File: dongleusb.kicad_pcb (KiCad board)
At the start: 2 copper layers, 13 parts, among them P7 UART_GROVE, U1 FT230XS, U2 HM-11

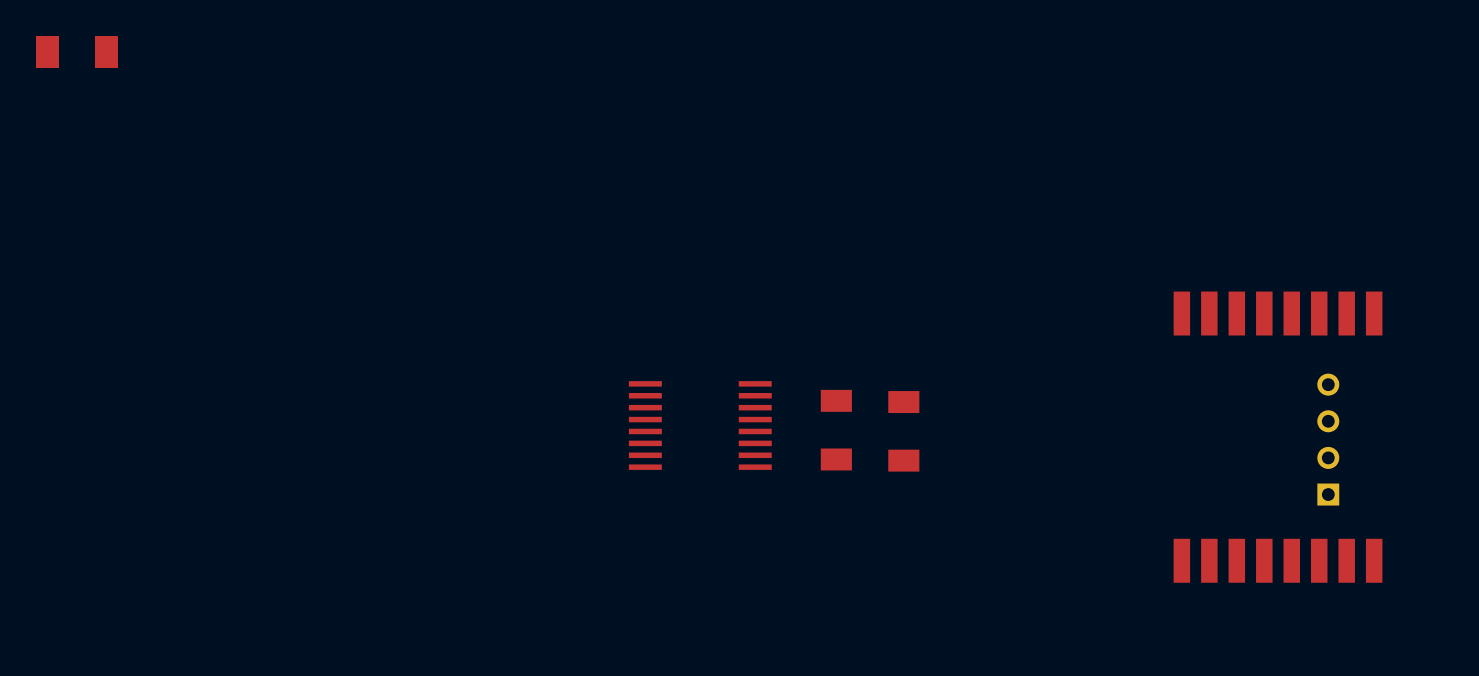
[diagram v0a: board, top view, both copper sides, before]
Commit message: Added LEDs informations. Added USB footprint. Placed some components into layout.
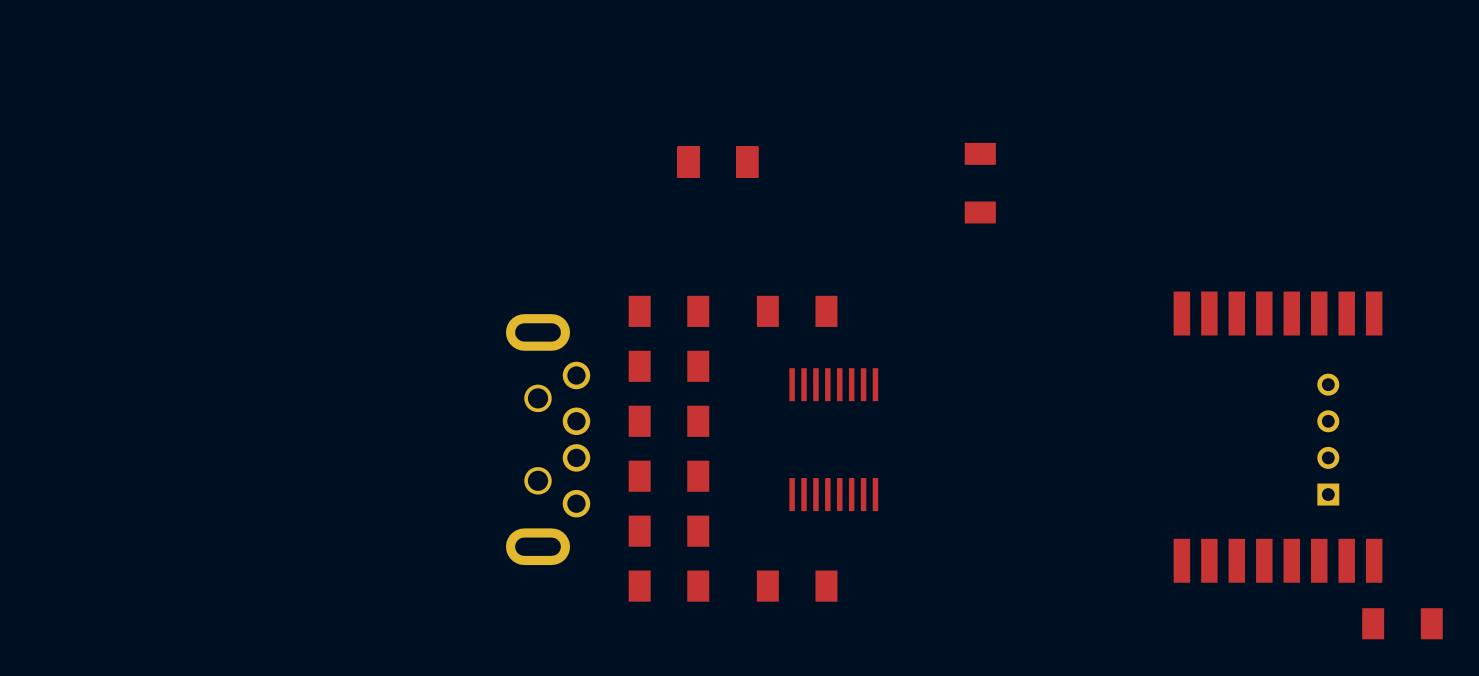
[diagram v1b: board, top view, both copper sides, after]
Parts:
- added D1: LED, W-LED-1206, F.Cu at (178.1, 107.1)
- added D2: LED, W-LED-1206, F.Cu at (138.0, 90.0)
- added D3: LED, W-LED-1206, F.Cu at (138.0, 105.0)
- added P1: USB, W-CONN-USB-A-MULTICOMP-THT, F.Cu at (123.0, 97.0)
- moved R5 49.0 mm to (145.0, 105.0)
- moved C1 41.6 mm to (138.0, 102.0)
- moved R1 39.8 mm to (138.0, 99.0)
- moved C2 38.1 mm to (138.0, 96.0)
- moved R2 36.6 mm to (138.0, 93.0)
- moved C4 35.5 mm to (140.7, 81.8)
- moved R3 35.5 mm to (140.7, 81.8)
- moved R6 35.5 mm to (140.7, 81.8)
- moved C3 14.2 mm to (155.0, 83.0)
- moved U1 7.33 mm to (147.0, 97.0), turned to 0 degrees
- moved R4 6.83 mm to (145.0, 90.0), turned to 0 degrees

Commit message: Placed all components. Added some commercial informations of communications modules.
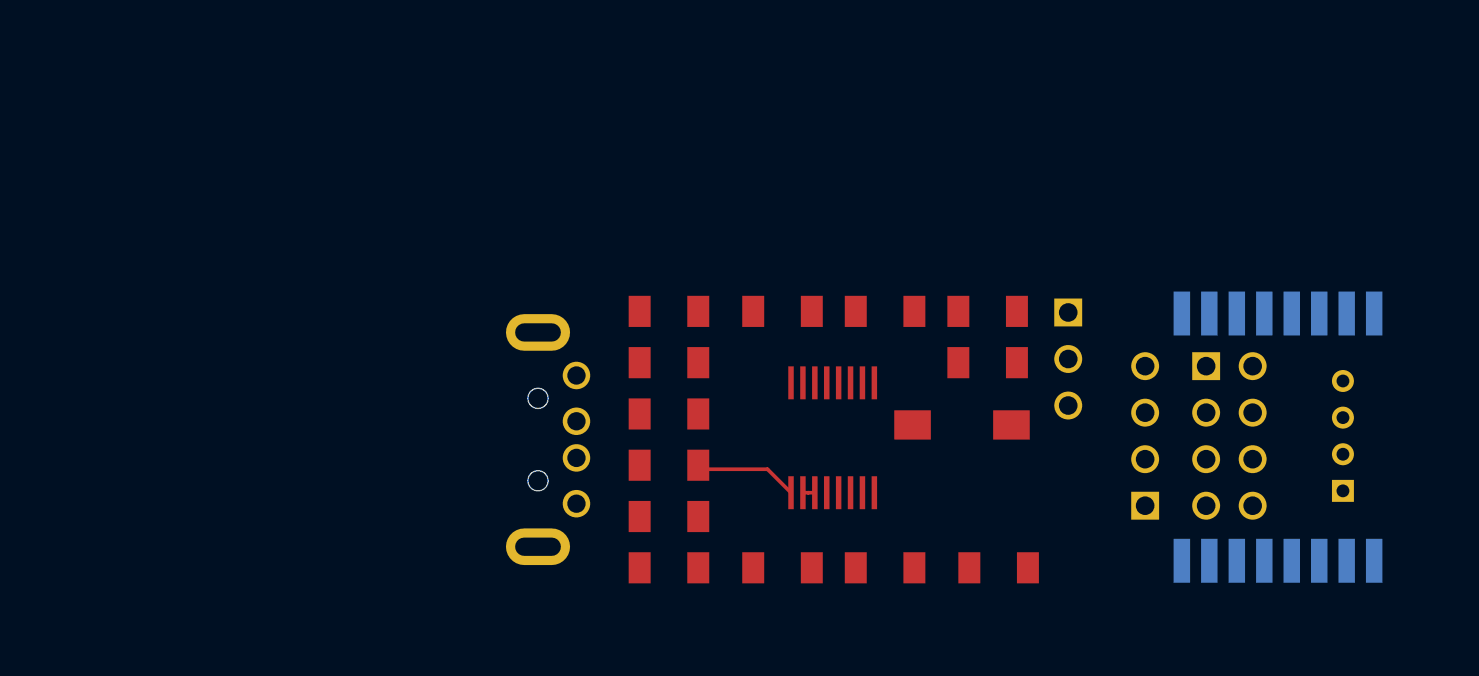
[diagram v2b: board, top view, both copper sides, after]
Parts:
- added G***: OSHW-logo_silkscreen-front_3mm, OSHW-logo_silkscreen-front_3mm, F.Cu at (160.0, 99.4)
- added JP1: ENABLE_VCC, W-CONN-3x1-STRIP, F.Cu at (159.8, 92.6)
- added P5: ESP8266, W-CONN-4x2-STRIP, F.Cu at (168.6, 96.8)
- added P6: UART_TERMINAL, W-CONN-4x1-STRIP, F.Cu at (164.0, 96.8)
- added SW1: RESET, W-SWITCH-EVQPE1, F.Cu at (154.0, 96.2)
- U2: moved to B.Cu
- moved R3 24.0 mm to (149.8, 104.0), turned to 180 degrees
- moved D1 22.3 mm to (156.0, 104.0), turned to 180 degrees
- moved C4 18.4 mm to (155.4, 92.8), turned to 180 degrees
- moved R6 16.8 mm to (155.4, 90.0), turned to 180 degrees
- moved R5 15.0 mm to (144.2, 90.0)
- moved D3 15.0 mm to (138.0, 90.0)
- moved R4 14.0 mm to (144.2, 104.0)
- moved D2 14.0 mm to (138.0, 104.0)
- moved C3 8.72 mm to (149.8, 90.0), turned to 0 degrees
- moved P7 0.82 mm to (174.8, 96.8)
- moved C1 0.80 mm to (138.0, 101.2)
- moved R1 0.60 mm to (138.0, 98.4)
- moved C2 0.40 mm to (138.0, 95.6)
- moved R2 0.20 mm to (138.0, 92.8)
- moved U1 0.12 mm to (146.9, 96.9), turned to 180 degrees
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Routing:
- net N-0000031: track 0.00 -> 5.60 mm
- net +3.3V: track 0.00 -> 0.65 mm
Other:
- net class Default: clearance 0.254 -> 0.2; trace_width 0.254 -> 0.2; via_dia 0.889 -> 0.8; via_drill 0.635 -> 0.4
- rule trace_clearance: 0.254 -> 0.2
- rule trace_min: 0.254 -> 0.2
- rule via_min_drill: 0.508 -> 0.4
- rule via_min_size: 0.889 -> 0.8
- board text added: "A"
- board text added: "B"
- board text added: "W001-0 USB2World CC 4.0 BY-SA"

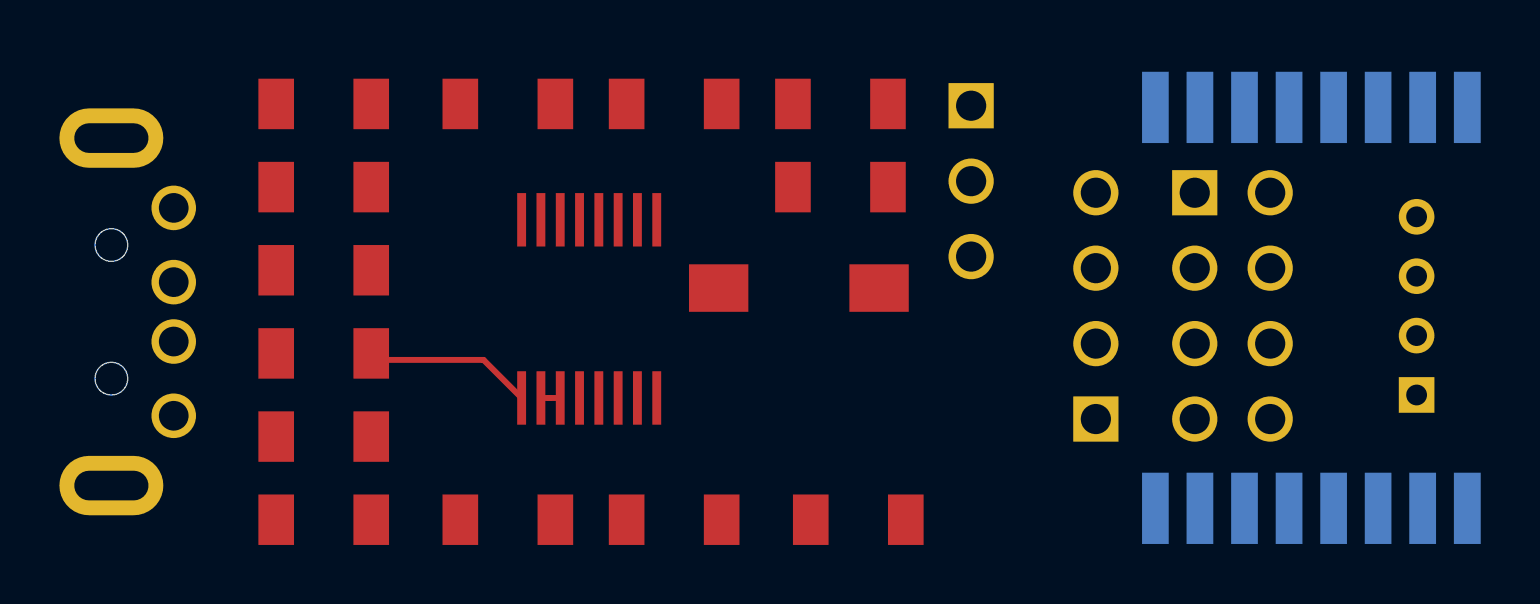
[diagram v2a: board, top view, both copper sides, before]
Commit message: Connected all nets into layout.
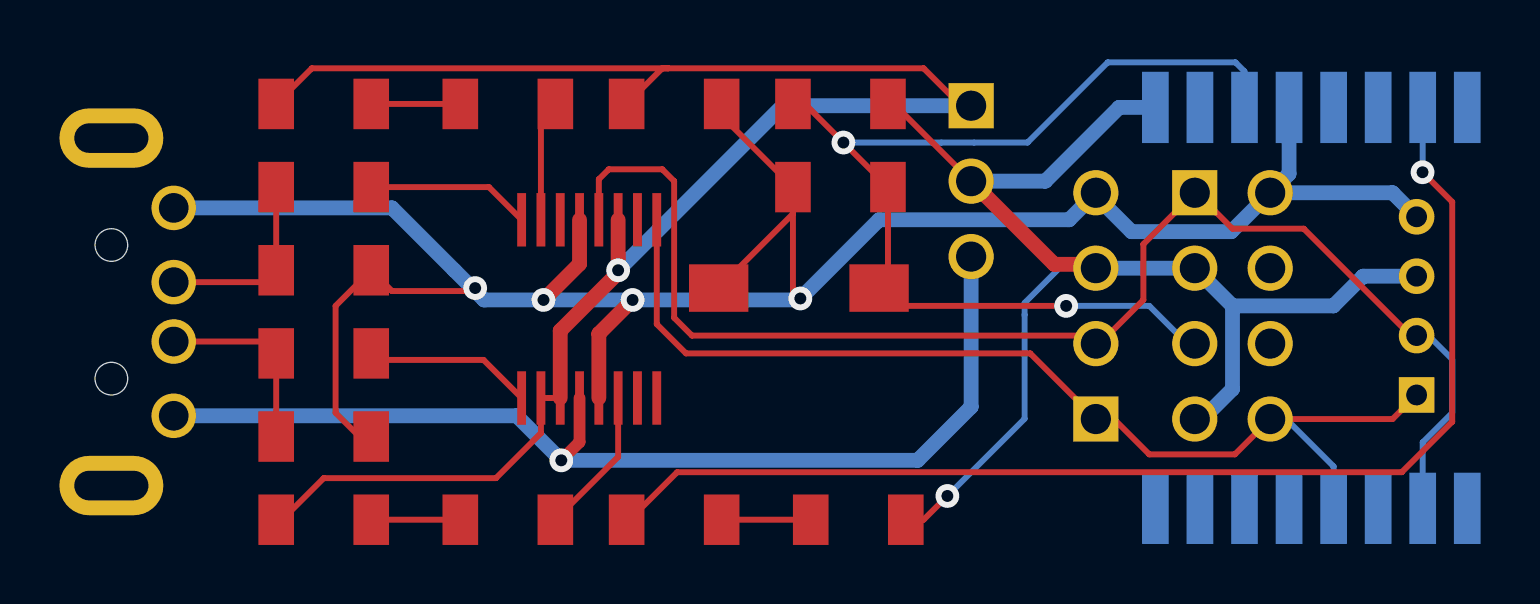
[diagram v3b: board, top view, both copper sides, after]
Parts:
- moved G*** 4.70 mm to (162.3, 103.5)
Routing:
- net GND: track 0.00 -> 79.0 mm, vias 0 -> 4
- net +3.3V: track 0.65 -> 59.3 mm, vias 0 -> 1
- net /UART_TX: track 0.00 -> 46.3 mm
- net /VCC: track 0.00 -> 44.9 mm, vias 0 -> 1
- net /LED_COMM: track 0.00 -> 40.2 mm, vias 0 -> 1
- net /UART_RX: track 0.00 -> 36.0 mm
- net +5V: track 0.00 -> 35.6 mm, vias 0 -> 1
- net /RESET: track 0.00 -> 35.3 mm, vias 0 -> 2
- net N-0000033: track 0.00 -> 6.42 mm
- net N-0000030: track 0.00 -> 6.42 mm
- net N-0000032: track 0.00 -> 5.52 mm
- net N-0000018: track 0.00 -> 4.97 mm
- net N-0000017: track 0.00 -> 4.10 mm
- net N-0000021: track 0.00 -> 3.00 mm
- net N-0000019: track 0.00 -> 3.00 mm
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
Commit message: Added my logo
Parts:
- added VAL: REF, W-LOGO-4MM, F.Cu at (160.1, 99.0)
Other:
- rule pad_to_mask_clearance: 0 -> 0.1
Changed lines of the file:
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@@
     (tracks 176)
     (zones 0)
-    (modules 22)
+    (modules 23)
     (nets 18)
   )
@@
     (pad_size 1.524 1.524)
     (pad_drill 1.016)
-    (pad_to_mask_clearance 0)
+    (pad_to_mask_clearance 0.1)
+    (solder_mask_min_width 0.1)
     (aux_axis_origin 0 0)
     (visible_elements 7FFFFFBF)
@@
       (psa4output false)
       (plotreference true)
-      (plotvalue true)
+      (plotvalue false)
       (plotothertext true)
       (plotinvisibletext false)
-      (padsonsilk true)
+      (padsonsilk false)
       (subtractmaskfromsilk false)
-      (outputformat 5)
+      (outputformat 1)
       (mirror false)
       (drillshape 0)
@@
       (xy -0.90932 1.3462)) (layer Serigrafia.Fronte) (width 0.00254))
   )
+  (module W-LOGO-4MM (layer Rame.Fronte)
+    (at 160.1 99)
+    (fp_text reference VAL (at 0 0) (layer Serigrafia.Fronte) hide
+      (effects (font (size 0.381 0.381) (thickness 0.127)))
+    )
+    (fp_text value REF (at 0 0) (layer Serigrafia.Fronte) hide
+      (effects (font (size 0.381 0.381) (thickness 0.127)))
+    )
+    (fp_poly (pts (xy 1.90754 -0.00508) (xy 1.89738 0.20066) (xy 1.8669 0.40132) (xy 1.8161 0.5969)
+      (xy 1.74244 0.7874) (xy 1.64846 0.96774) (xy 1.53416 1.13538) (xy 1.44018 1.24714)
+      (xy 1.44018 1.01092) (xy 1.43764 0.99568) (xy 1.43002 0.96012) (xy 1.41732 0.90424)
+      (xy 1.39954 0.82804) (xy 1.37922 0.73914) (xy 1.35636 0.63246) (xy 1.32842 0.51562)
+      (xy 1.30048 0.38862) (xy 1.27 0.25146) (xy 1.23698 0.10922) (xy 1.20142 -0.0381)
+      (xy 1.1684 -0.18796) (xy 1.13284 -0.34036) (xy 1.09982 -0.49022) (xy 1.06426 -0.63754)
+      (xy 1.03124 -0.77978) (xy 1.00076 -0.9144) (xy 0.97028 -1.0414) (xy 0.94488 -1.1557)
+      (xy 0.91948 -1.25984) (xy 0.89916 -1.34874) (xy 0.88138 -1.4224) (xy 0.86868 -1.47574)
+      (xy 0.86106 -1.50876) (xy 0.85852 -1.52146) (xy 0.84582 -1.51892) (xy 0.81788 -1.50368)
+      (xy 0.7747 -1.48082) (xy 0.7239 -1.45034) (xy 0.70612 -1.44018) (xy 0.64262 -1.40208)
+      (xy 0.59944 -1.37414) (xy 0.57404 -1.35382) (xy 0.56388 -1.33858) (xy 0.56134 -1.3335)
+      (xy 0.56642 -1.31826) (xy 0.57404 -1.28016) (xy 0.58674 -1.22428) (xy 0.60452 -1.14808)
+      (xy 0.62738 -1.05664) (xy 0.65278 -0.9525) (xy 0.68072 -0.83312) (xy 0.7112 -0.70612)
+      (xy 0.74422 -0.5715) (xy 0.76962 -0.47498) (xy 0.80264 -0.33528) (xy 0.83566 -0.2032)
+      (xy 0.8636 -0.07874) (xy 0.89154 0.03302) (xy 0.9144 0.13208) (xy 0.93472 0.2159)
+      (xy 0.94996 0.28448) (xy 0.96266 0.33528) (xy 0.96774 0.36322) (xy 0.97028 0.37084)
+      (xy 0.96012 0.36322) (xy 0.93472 0.3429) (xy 0.89154 0.3048) (xy 0.8382 0.25654)
+      (xy 0.76962 0.19558) (xy 0.69342 0.12446) (xy 0.60452 0.04572) (xy 0.508 -0.04318)
+      (xy 0.4064 -0.13716) (xy 0.30734 -0.22606) (xy -0.35052 -0.83312) (xy -0.40132 -0.80264)
+      (xy -0.43688 -0.77978) (xy -0.44704 -0.75946) (xy -0.44704 -0.75438) (xy -0.43942 -0.72136)
+      (xy -0.42926 -0.67056) (xy -0.41402 -0.59944) (xy -0.3937 -0.51562) (xy -0.37338 -0.4191)
+      (xy -0.34798 -0.31242) (xy -0.32258 -0.19558) (xy -0.29718 -0.0762) (xy -0.26924 0.04826)
+      (xy -0.2413 0.17272) (xy -0.21336 0.29718) (xy -0.18796 0.4191) (xy -0.16256 0.5334)
+      (xy -0.1397 0.64008) (xy -0.11684 0.7366) (xy -0.09906 0.82042) (xy -0.08382 0.889)
+      (xy -0.07366 0.9398) (xy -0.06604 0.97028) (xy -0.06604 0.98044) (xy -0.0762 0.97282)
+      (xy -0.1016 0.94996) (xy -0.1397 0.91186) (xy -0.19558 0.86106) (xy -0.26162 0.79756)
+      (xy -0.33782 0.7239) (xy -0.42418 0.64262) (xy -0.51816 0.55118) (xy -0.61722 0.45466)
+      (xy -0.70866 0.3683) (xy -0.8128 0.2667) (xy -0.91186 0.17272) (xy -1.00584 0.08382)
+      (xy -1.0922 0.00254) (xy -1.1684 -0.07112) (xy -1.23444 -0.13208) (xy -1.28524 -0.18288)
+      (xy -1.32588 -0.21844) (xy -1.34874 -0.2413) (xy -1.3589 -0.24638) (xy -1.37414 -0.2413)
+      (xy -1.40462 -0.22352) (xy -1.44526 -0.20066) (xy -1.49352 -0.17526) (xy -1.54178 -0.14478)
+      (xy -1.58496 -0.11938) (xy -1.62052 -0.09398) (xy -1.64084 -0.07874) (xy -1.64592 -0.07112)
+      (xy -1.6383 -0.0635) (xy -1.61036 -0.0381) (xy -1.56972 0.00254) (xy -1.51384 0.05334)
+      (xy -1.4478 0.11684) (xy -1.36906 0.1905) (xy -1.28016 0.27178) (xy -1.18364 0.36068)
+      (xy -1.08204 0.45466) (xy -0.97536 0.55372) (xy -0.8636 0.65786) (xy -0.7493 0.762)
+      (xy -0.635 0.86868) (xy -0.5207 0.97282) (xy -0.40894 1.07442) (xy -0.30226 1.17348)
+      (xy -0.19812 1.26746) (xy -0.1016 1.35636) (xy -0.0127 1.43764) (xy 0.06604 1.5113)
+      (xy 0.13462 1.5748) (xy 0.19304 1.6256) (xy 0.23622 1.6637) (xy 0.26416 1.6891)
+      (xy 0.27432 1.69672) (xy 0.27432 1.69672) (xy 0.2921 1.69164) (xy 0.32004 1.6764)
+      (xy 0.32766 1.67386) (xy 0.35306 1.65608) (xy 0.36068 1.6383) (xy 0.35814 1.60782)
+      (xy 0.3556 1.60274) (xy 0.35052 1.58242) (xy 0.3429 1.53924) (xy 0.3302 1.47828)
+      (xy 0.31242 1.39954) (xy 0.2921 1.3081) (xy 0.26924 1.20396) (xy 0.24638 1.0922)
+      (xy 0.22098 0.97282) (xy 0.19304 0.8509) (xy 0.16764 0.72644) (xy 0.14224 0.60452)
+      (xy 0.1143 0.48514) (xy 0.09144 0.37338) (xy 0.06858 0.26924) (xy 0.04826 0.1778)
+      (xy 0.03302 0.09906) (xy 0.02032 0.0381) (xy 0.01016 -0.00508) (xy 0.00762 -0.02286)
+      (xy -0.00254 -0.0635) (xy -0.00508 -0.08382) (xy 0 -0.0889) (xy 0.01016 -0.08382)
+      (xy 0.01016 -0.08128) (xy 0.02286 -0.07112) (xy 0.05334 -0.04572) (xy 0.09652 -0.00762)
+      (xy 0.15748 0.04318) (xy 0.2286 0.10668) (xy 0.30988 0.1778) (xy 0.40132 0.25654)
+      (xy 0.50292 0.3429) (xy 0.60706 0.43434) (xy 0.69342 0.508) (xy 1.35382 1.08204)
+      (xy 1.397 1.05664) (xy 1.42494 1.03632) (xy 1.43764 1.016) (xy 1.44018 1.01092)
+      (xy 1.44018 1.24714) (xy 1.40208 1.29286) (xy 1.24968 1.4351) (xy 1.08458 1.55956)
+      (xy 0.93218 1.651) (xy 0.76708 1.7272) (xy 0.59436 1.7907) (xy 0.42418 1.83642)
+      (xy 0.39624 1.8415) (xy 0.31496 1.85166) (xy 0.21844 1.85928) (xy 0.11176 1.86436)
+      (xy 0.00508 1.86436) (xy -0.09652 1.86182) (xy -0.18288 1.8542) (xy -0.20828 1.85166)
+      (xy -0.41656 1.80848) (xy -0.61722 1.74244) (xy -0.80772 1.65354) (xy -0.98806 1.54178)
+      (xy -1.1557 1.4097) (xy -1.25476 1.31572) (xy -1.39446 1.16078) (xy -1.5113 0.9906)
+      (xy -1.61036 0.80772) (xy -1.68656 0.61468) (xy -1.74244 0.41656) (xy -1.77546 0.21082)
+      (xy -1.78562 0.03302) (xy -1.77292 -0.1778) (xy -1.73736 -0.381) (xy -1.68148 -0.57912)
+      (xy -1.60528 -0.76454) (xy -1.50876 -0.94234) (xy -1.39446 -1.1049) (xy -1.26238 -1.25476)
+      (xy -1.11506 -1.39192) (xy -0.95504 -1.5113) (xy -0.77978 -1.6129) (xy -0.59182 -1.69672)
+      (xy -0.3937 -1.76022) (xy -0.2032 -1.79832) (xy -0.12954 -1.80594) (xy -0.04064 -1.81102)
+      (xy 0.05842 -1.81102) (xy 0.15748 -1.81102) (xy 0.24638 -1.80594) (xy 0.32258 -1.79832)
+      (xy 0.32512 -1.79832) (xy 0.5334 -1.75514) (xy 0.73152 -1.6891) (xy 0.91948 -1.60274)
+      (xy 1.09474 -1.4986) (xy 1.2573 -1.37668) (xy 1.40462 -1.23698) (xy 1.5367 -1.0795)
+      (xy 1.651 -0.90932) (xy 1.74498 -0.72898) (xy 1.81864 -0.5334) (xy 1.85166 -0.4191)
+      (xy 1.88976 -0.21082) (xy 1.90754 -0.00508) (xy 1.90754 -0.00508)) (layer Serigrafia.Fronte) (width 0.00254))
+  )
   (gr_text "W001-0\nUSB2World\nCC 4.0 BY-SA" (at 150 98.8) (layer Serigrafia.Fronte)
